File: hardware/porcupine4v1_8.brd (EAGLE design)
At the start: 24.4 x 27.4 mm, 33 parts, among them X1 PROGCON

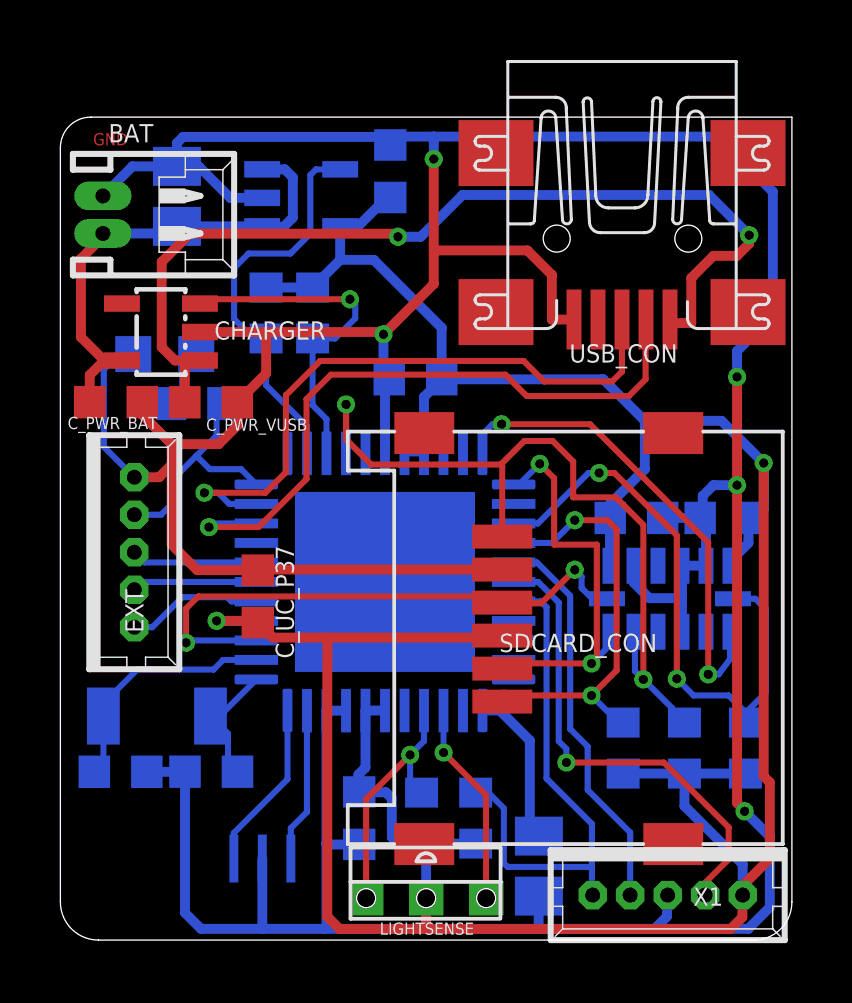
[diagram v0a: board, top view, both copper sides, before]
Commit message: updated porcupine4v1_8: fixed 12MHZ resonator board footprint
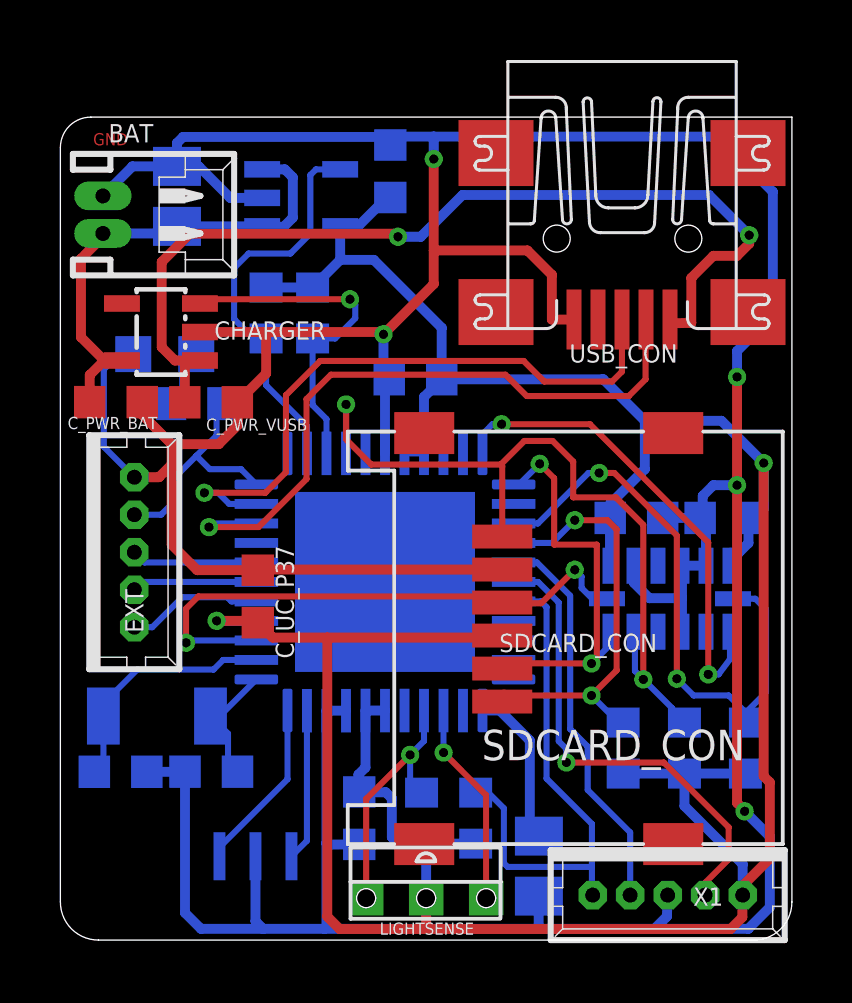
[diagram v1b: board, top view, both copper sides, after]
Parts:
- 12MHZ_RESONATOR: value RESONATORPRQC-S -> RESONATORPRQC-C; device jnode:PRQC -> HedgehogLib:PRQC-C
- moved 12MHZ_RESONATOR 0.24 mm to (6.50, 2.79)
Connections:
- net GND: now also 12MHZ_RESONATOR.2_GND; no longer 12MHZ_RESONATOR.GND
- net N$1: now also 12MHZ_RESONATOR.3; no longer 12MHZ_RESONATOR.2
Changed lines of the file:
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@@
 <grid distance="1" unitdist="mil" unit="mil" style="dots" multiple="10" display="yes" altdistance="1" altunitdist="mil" altunit="mil"/>
 <layers>
-<layer number="1" name="Top" color="4" fill="1" visible="no" active="yes"/>
-<layer number="16" name="Bottom" color="1" fill="1" visible="no" active="yes"/>
-<layer number="17" name="Pads" color="2" fill="1" visible="no" active="yes"/>
-<layer number="18" name="Vias" color="2" fill="1" visible="no" active="yes"/>
-<layer number="19" name="Unrouted" color="6" fill="1" visible="no" active="yes"/>
+<layer number="1" name="Top" color="4" fill="1" visible="yes" active="yes"/>
+<layer number="16" name="Bottom" color="1" fill="1" visible="yes" active="yes"/>
+<layer number="17" name="Pads" color="2" fill="1" visible="yes" active="yes"/>
+<layer number="18" name="Vias" color="2" fill="1" visible="yes" active="yes"/>
+<layer number="19" name="Unrouted" color="6" fill="1" visible="yes" active="yes"/>
 <layer number="20" name="Dimension" color="15" fill="1" visible="yes" active="yes"/>
 <layer number="21" name="tPlace" color="7" fill="1" visible="yes" active="yes"/>
-<layer number="22" name="bPlace" color="7" fill="1" visible="no" active="yes"/>
+<layer number="22" name="bPlace" color="7" fill="1" visible="yes" active="yes"/>
 <layer number="23" name="tOrigins" color="15" fill="1" visible="yes" active="yes"/>
-<layer number="24" name="bOrigins" color="15" fill="1" visible="no" active="yes"/>
+<layer number="24" name="bOrigins" color="15" fill="1" visible="yes" active="yes"/>
 <layer number="25" name="tNames" color="7" fill="1" visible="yes" active="yes"/>
-<layer number="26" name="bNames" color="7" fill="1" visible="no" active="yes"/>
+<layer number="26" name="bNames" color="7" fill="1" visible="yes" active="yes"/>
 <layer number="27" name="tValues" color="7" fill="1" visible="no" active="yes"/>
 <layer number="28" name="bValues" color="7" fill="1" visible="no" active="yes"/>
@@
 <attribute name="VALUE" x="13.9446" y="4.699" size="1.27" layer="28" rot="MR270"/>
 </element>
-<element name="12MHZ_RESONATOR" library="jnode" package="PRQC" value="RESONATORPRQC-S" x="6.731" y="2.7178" smashed="yes" rot="MR180">
-<attribute name="DIGIKEY" value="http://www.digikey.com/product-detail/en/PRQC12.00CR5010X000/478-6318-1-ND/2506334" x="6.731" y="2.7178" size="1.778" layer="28" rot="MR180" display="off"/>
-</element>
 <element name="32KHZ_CRYSTAL" library="HedgehogLib" package="SMD_CRYSTAL" value="SMD_CRYSTAL" x="3.2258" y="7.4676" rot="MR0"/>
 <element name="R7" library="rcl" package="R0603" value="10k" x="6.858" y="20.9042" smashed="yes" rot="MR90">
@@
 <attribute name="VALUE" x="1.9798" y="21.5326" size="1.27" layer="28" rot="MR180"/>
 </element>
+<element name="12MHZ_RESONATOR" library="HedgehogLib" package="PRQC-C" value="RESONATORPRQC-C" x="6.5024" y="2.794" rot="MR180"/>
 </elements>
 <signals>
@@
 <wire x1="15.637" y1="1.4638" x2="15.5702" y2="1.397" width="0.3302" layer="16"/>
 <wire x1="15.9512" y1="1.4638" x2="15.637" y2="1.4638" width="0.3302" layer="16"/>
-<wire x1="6.731" y1="0.3756" x2="8.8138" y2="0.3756" width="0.3302" layer="16"/>
+<wire x1="4.6876" y1="0.3756" x2="6.7564" y2="0.3756" width="0.3302" layer="16"/>
+<wire x1="6.7564" y1="0.3756" x2="8.8138" y2="0.3756" width="0.3302" layer="16"/>
 <wire x1="8.8138" y1="0.3756" x2="15.9418" y2="0.3756" width="0.3302" layer="16"/>
 <wire x1="21.4438" y1="13.8254" x2="21.52" y2="13.8254" width="0.2032" layer="16"/>
@@
 <via x="22.5552" y="18.7706" extent="1-16" drill="0.3048" shape="octagon"/>
 <via x="22.8092" y="4.2926" extent="1-16" drill="0.3048" shape="octagon"/>
-<contactref element="12MHZ_RESONATOR" pad="GND"/>
 <wire x1="16.383" y1="20.6844" x2="16.383" y2="22.1742" width="0.3302" layer="1"/>
 <wire x1="16.383" y1="22.1742" x2="15.5702" y2="22.987" width="0.3302" layer="1"/>
@@
 <wire x1="2.8816" y1="5.6096" x2="4.1796" y2="5.6096" width="0.3302" layer="16"/>
 <wire x1="4.1542" y1="5.6134" x2="4.1796" y2="5.6096" width="0.3302" layer="16"/>
-<wire x1="4.6876" y1="0.3756" x2="6.731" y2="0.3756" width="0.3302" layer="16"/>
-<wire x1="6.731" y1="2.7178" x2="6.731" y2="0.3756" width="0.3302" layer="16"/>
 <wire x1="10.8204" y1="16.2255" x2="10.8204" y2="18.556" width="0.3302" layer="16"/>
 <wire x1="3.9022" y1="26.0952" x2="3.8862" y2="25.7904" width="0.3302" layer="16"/>
@@
 <wire x1="9.9612" y1="3.189" x2="8.9096" y2="3.1836" width="0.3302" layer="16"/>
 <wire x1="8.9096" y1="3.1836" x2="8.8674" y2="3.2258" width="0.3302" layer="16"/>
+<contactref element="12MHZ_RESONATOR" pad="2_GND"/>
+<wire x1="6.5024" y1="2.794" x2="6.5024" y2="0.6296" width="0.3302" layer="16"/>
+<wire x1="6.5024" y1="0.6296" x2="6.7564" y2="0.3756" width="0.3302" layer="16"/>
 </signal>
 <signal name="USB_D+@RC5">
@@
 <signal name="N$1">
 <contactref element="PIC_CONTROLLER" pad="32"/>
-<contactref element="12MHZ_RESONATOR" pad="2"/>
-<wire x1="8.2184" y1="4.2672" x2="8.2184" y2="7.6455" width="0.2032" layer="16"/>
-<wire x1="7.681" y1="2.7178" x2="7.681" y2="3.7298" width="0.2032" layer="16"/>
-<wire x1="7.681" y1="3.7298" x2="8.2184" y2="4.2672" width="0.2032" layer="16"/>
+<contactref element="12MHZ_RESONATOR" pad="3"/>
+<wire x1="8.2184" y1="7.6455" x2="8.2184" y2="3.31" width="0.2032" layer="16"/>
+<wire x1="8.2184" y1="3.31" x2="7.7024" y2="2.794" width="0.2032" layer="16"/>
 </signal>
 <signal name="N$2">
 <contactref element="PIC_CONTROLLER" pad="33"/>
+<wire x1="5.3024" y1="3.0926" x2="7.5704" y2="5.3606" width="0.2032" layer="16"/>
+<wire x1="7.5704" y1="5.3606" x2="7.5704" y2="7.6535" width="0.2032" layer="16"/>
 <contactref element="12MHZ_RESONATOR" pad="1"/>
-<wire x1="5.781" y1="2.7178" x2="5.781" y2="3.5712" width="0.2032" layer="16"/>
-<wire x1="5.781" y1="3.5712" x2="7.5704" y2="5.3606" width="0.2032" layer="16"/>
-<wire x1="7.5704" y1="5.3606" x2="7.5704" y2="7.6535" width="0.2032" layer="16"/>
+<wire x1="5.3024" y1="2.794" x2="5.3024" y2="3.0926" width="0.2032" layer="16"/>
 </signal>
 <signal name="L_GND@RE0">
